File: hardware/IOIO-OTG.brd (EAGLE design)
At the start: 68.6 x 30.5 mm, 60 parts, among them Q1 IRLML2244, Q2 2N7002PW, Q3 AO3404A, U1 PIC24FJ256GB206, U14 SWITCH_SPDT, U2 TPS62133RGTT, U3 VREG_MIC5216

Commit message: v22a in copper and sch
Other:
- board text added: "v22a"
- board text removed: "v22"
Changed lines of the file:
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@@
 <circle x="55.88" y="29.21" radius="1.1039" width="0.508" layer="22"/>
 <circle x="53.34" y="29.21" radius="1.1039" width="0.508" layer="22"/>
-<text x="67.9958" y="7.4676" size="1.016" layer="16" font="vector" ratio="20" rot="SMR270">v22</text>
+<text x="67.9958" y="7.4676" size="1.016" layer="16" font="vector" ratio="20" rot="SMR270">v22a</text>
 <wire x1="57.15" y1="30.48" x2="59.69" y2="30.48" width="0.3048" layer="21"/>
 <wire x1="59.69" y1="27.94" x2="59.69" y2="30.48" width="0.3048" layer="21"/>

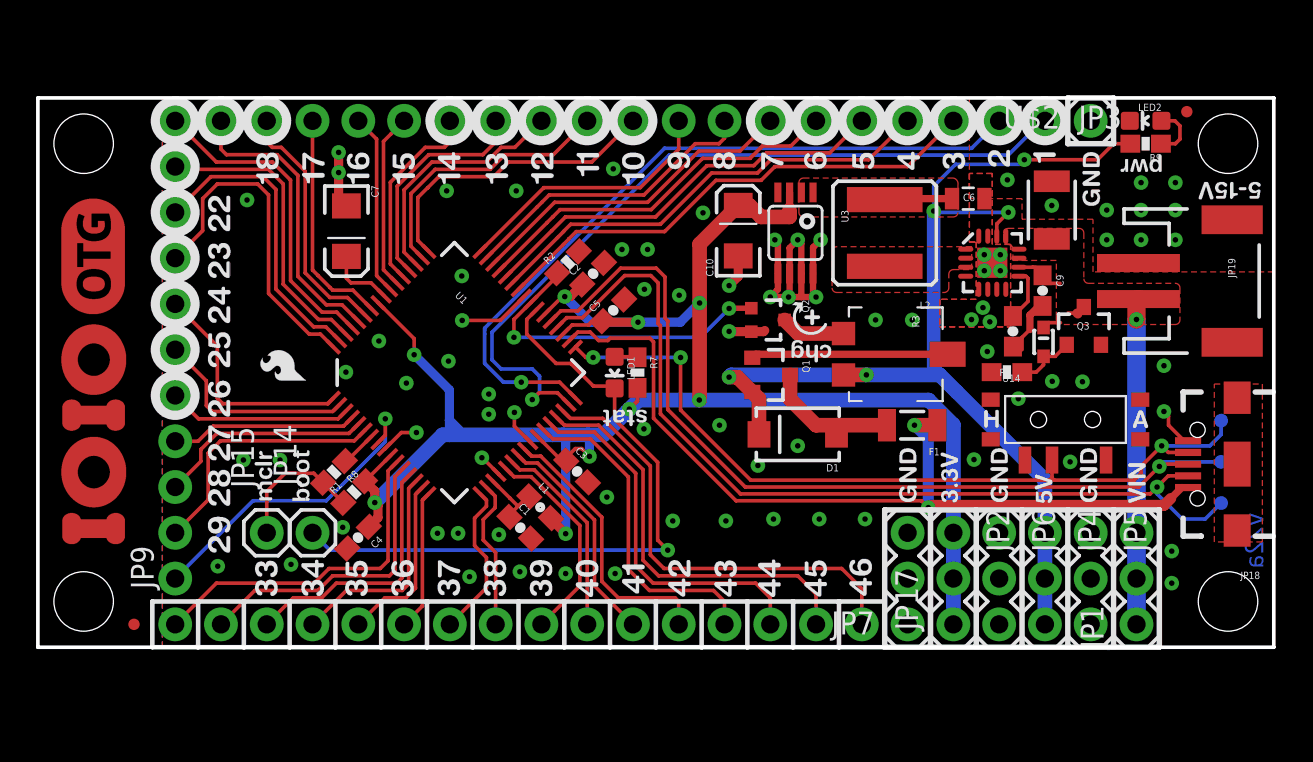
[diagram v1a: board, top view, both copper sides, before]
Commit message: copied from v22b @ commit: 'Seed Logo'
needed to copy in v22b, because a lot of work was done to v22b, and we
want to keep these two branches parallel
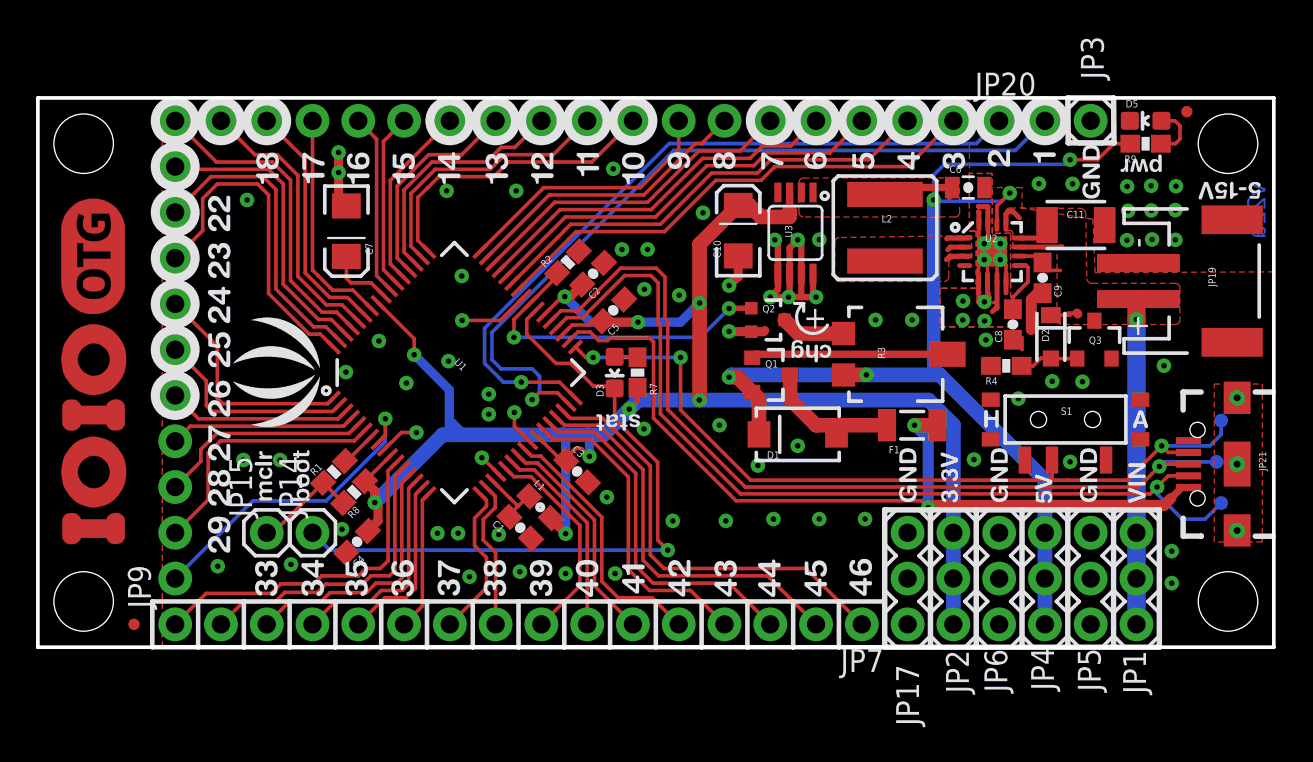
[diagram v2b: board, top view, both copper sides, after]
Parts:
- removed JP18: (no value), SparkFun-Connectors:USB-B-MICRO-SMD_V03
- removed LOGO2: SFE_LOGO_FLAME.1_INCH, SparkFun-Aesthetics:SFE_LOGO_FLAME_.1
- removed LOGO4: SFE_LOGO_NAME_FLAME.1_INCH, SparkFun-Aesthetics:SFE_LOGO_NAME_FLAME_.1
- added JP21: AB MICRO USB, SparkFun-Connectors:USB-AB-MICRO-SMD_V03
- added U$13: (no value), Logo:LOGO_SILK
- added U$15: (no value), Logo:SMALL_SEEED_LOGO
- C10: device SparkFun-Passives:EIA3216 -> SparkFun-Capacitors:EIA3216
- C11: device SparkFun-Passives:1210 -> SparkFun-Capacitors:1210
- C6: device SparkFun-Passives:0805 -> SparkFun-Capacitors:0805-CAP
- C7: device SparkFun:EIA3216 -> SparkFun-Capacitors:EIA3216
- D2: device IOIO-OTG:SPARKFUN-DISCRETESEMI_SOD-523 -> SparkFun-DiscreteSemi:PANASONIC_SMINI2-F5-B
- F1: value PTCSMD -> 0.75A
- JP1: value VIN -> (none)
- JP14, JP15, JP3: value M01PTH -> (none)
- JP19: value JST Connector -> JST; device SparkFun:JST-2-SMD -> SparkFun-Connectors:JST-2-SMD
- JP20: value M191X19_NO_SILK -> (none)
- JP4: value 5V -> (none)
- JP7: value M161X16_NO_SILK -> (none)
- JP9: value M111X11_NO_SILK -> (none)
- Q3: value AO3404A -> MOSFET-NCHANNELAO3404A; device IOIO-OTG:SPARKFUN-DISCRETESEMI_SOT23-3 -> SparkFun-DiscreteSemi:SOT23-3
- U2: device SparkFun-PowerIC:QFN16-3X3MM -> SparkFun-PowerIC:QFN16-3X3MM_1:1_V03
- U3: value VREG_MIC5216 -> MIC5216
- moved C11 1.57 mm to (57.6, 23.4), turned to 0 degrees
- moved Q3 0.96 mm to (58.6, 17.0)
- moved C9 0.71 mm to (55.8, 20.5)
- moved C6 0.61 mm to (51.6, 25.5)
- moved U2 0.61 mm to (53.0, 22.0)
- moved D2 0.49 mm to (56.2, 17.2), turned to 270 degrees
- moved C8 0.38 mm to (54.1, 17.9)
- moved R4 0.35 mm to (53.7, 15.6)
- moved L2 0.29 mm to (47.0, 23.3)
- moved TP2 0.25 mm to (65.4, 10.3)
- moved C4 0.24 mm to (17.7, 5.85)
- renumbered LED1 to D3, LED2 to D5, U$2 to JP20, U14 to S1
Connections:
- net ANCHOR1: now also JP21.SHIELD1, JP21.SHIELD2, JP21.SHIELD3; no longer JP18.SHIELD1, JP18.SHIELD2, JP18.SHIELD3
- net D+: now also JP21.D+1; no longer JP18.D+1
- net D-: now also JP21.D-1; no longer JP18.D-1
- net GND: now also JP21.GND1; no longer JP18.GND1
- net USBID: now also JP21.ID1; no longer JP18.ID1
- net VBUS: now also JP21.VBUS1; no longer JP18.VBUS1
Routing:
- net GND: track 38.2 -> 52.1 mm, vias 81 -> 82
- net VIN: track 23.5 -> 28.5 mm
- net N$6: track 0.00 -> 3.14 mm
- net 5V: track 70.3 -> 67.9 mm
- net P7: track 7.64 -> 5.86 mm
- net PIN46: track 25.6 -> 24.4 mm
- net PIN45: track 23.1 -> 22.1 mm
- net PIN19: track 16.5 -> 15.5 mm
- net PIN44: track 20.7 -> 19.8 mm
- net PIN43: track 18.3 -> 17.5 mm
- net PIN42: track 15.4 -> 14.7 mm
- net PIN13: track 12.6 -> 11.9 mm
- net PIN14: track 11.0 -> 10.3 mm
- net PIN8: track 16.9 -> 16.4 mm
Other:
- board text added: "+"
- board text added: "Units are in inches"
- board text added: "www.seeedstudio.com"
